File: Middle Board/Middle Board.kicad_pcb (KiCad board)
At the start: 2 copper layers, 61 parts, among them J1 JTAG Connector, J2 Conn_Coaxial, J3 Conn_Coaxial, J4 Conn_Coaxial, J5 Conn_Coaxial, J6 Conn_02x10_Counter_Clockwise, SW1 SW_SPST, U1 ATSAMG55, U2 BNO055_Breakout, U3 MS5803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

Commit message: More changes
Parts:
- moved J4 45.7 mm to (156.2, 72.0)
- moved J5 45.1 mm to (166.8, 72.0)
- moved U6 5.66 mm to (163.0, 81.0)
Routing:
- added copper zone on F.Cu, net GND
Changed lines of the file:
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@@
     (47 F.CrtYd user)
     (48 B.Fab user hide)
-    (49 F.Fab user)
+    (49 F.Fab user hide)
   )
   (setup
@@
       (effects (font (size 1 1) (thickness 0.15)))
     )
-    (fp_text value B39162B3520U410 (at 0 -3) (layer F.Fab)
+    (fp_text value B39162B3520U410 (at 0 0) (layer F.Fab)
       (effects (font (size 1 1) (thickness 0.15)))
     )
@@
   )
   (module "Custom Footprints:SMA_SMD_RIGHT_ANGLE" (layer F.Cu)
-    (at 201 63 180)
+    (at 156.23 72 180)
     (fp_text reference J4 (at 6 -2 180) (layer F.SilkS)
       (effects (font (size 1 1) (thickness 0.15)))
@@
   )
   (module "Custom Footprints:SMA_SMD_RIGHT_ANGLE" (layer F.Cu)
-    (at 211 63 180)
+    (at 166.77 72 180)
     (fp_text reference J5 (at 6 -2 180) (layer F.SilkS)
       (effects (font (size 1 1) (thickness 0.15)))
@@
   )
   (module "Custom Footprints:SMD_PD_ANAREN" (layer F.Cu)
-    (at 159 77 90)
+    (at 163 81 90)
     (fp_text reference U6 (at 4 0 90) (layer F.SilkS)
       (effects (font (size 1 1) (thickness 0.15)))
@@
       )
     )
+  )
+  (zone (net 2) (net_name GND) (layer F.Cu) (hatch edge 0.508)
+    (connect_pads (clearance 0.153))
+    (min_thickness 0.254)
+    (fill yes (arc_segments 16) (thermal_gap 0.508) (thermal_bridge_width 0.508))
+    (polygon
+      (pts
+        (xy 120 72) (xy 120 90) (xy 153 90) (xy 153 72)
+      )
+    )

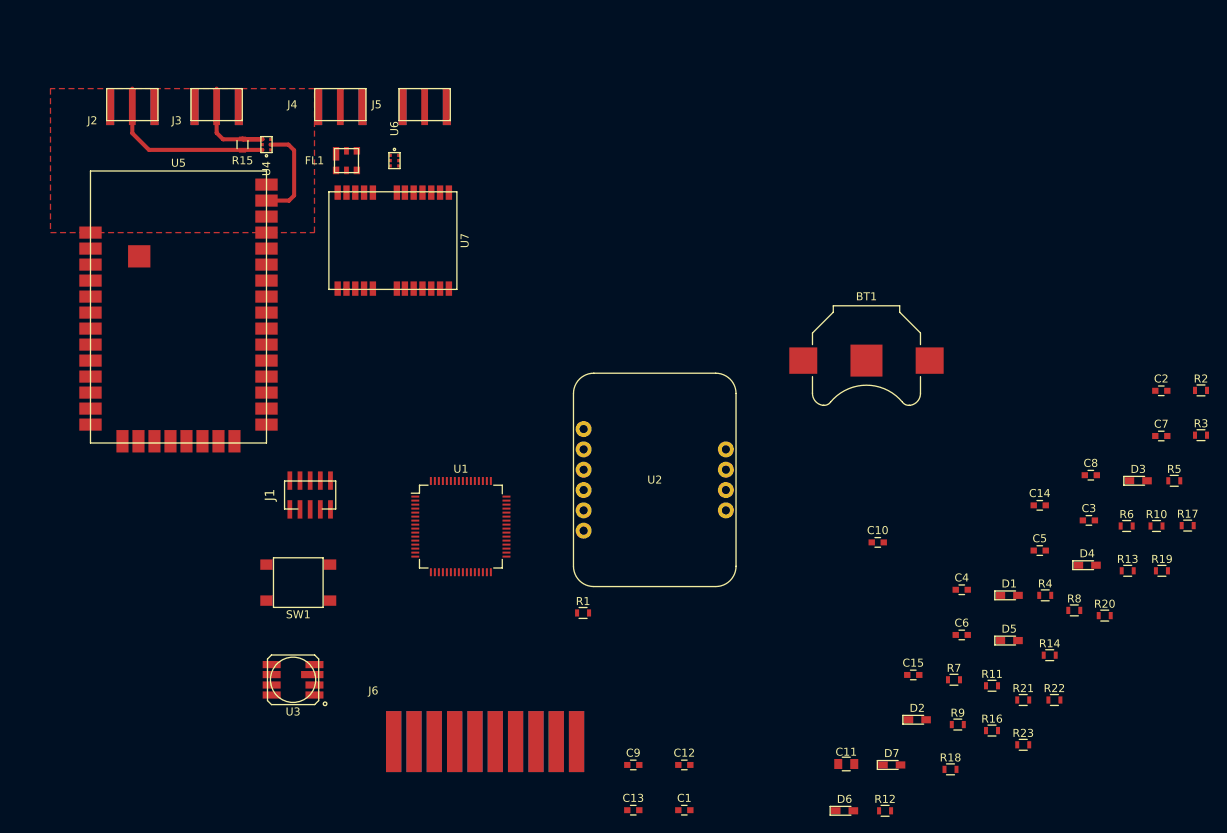
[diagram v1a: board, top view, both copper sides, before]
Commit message: Added the RS422 transceiver since I forgot it
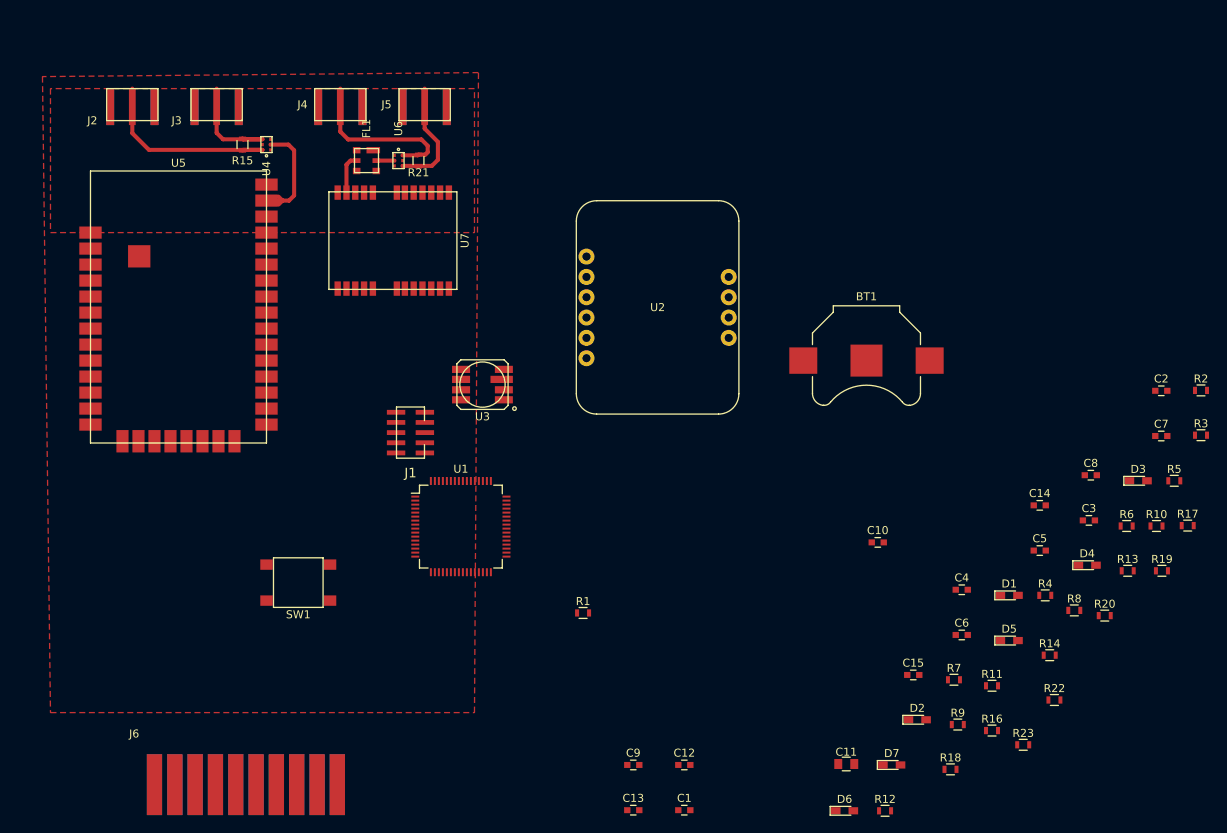
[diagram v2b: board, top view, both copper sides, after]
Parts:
- moved R21 101.3 mm to (166.0, 81.0), turned to 270 degrees
- moved U3 43.8 mm to (174.0, 109.0)
- moved J6 30.4 mm to (144.4, 162.8)
- moved U2 21.6 mm to (195.9, 99.3)
- moved J1 14.8 mm to (165.0, 115.0), turned to 90 degrees
- moved FL1 2.50 mm to (159.5, 81.0), turned to 270 degrees
- moved U6 0.50 mm to (163.5, 81.0)
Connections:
- U6 pad 1: Net-(U6-Pad1) -> GND
- U6 pad 3: Net-(U6-Pad1) -> GND
- U6 pad 5: Net-(U6-Pad1) -> GND
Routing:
- net /ANT3_RF_50Ω: track 0.00 -> 21.2 mm
- net /ANT4_RF_50Ω: track 0.00 -> 14.3 mm
- net /GPS_RF_50Ω: track 0.00 -> 4.71 mm
- net /ANT1_RF_50Ω: track 22.7 -> 25.2 mm
- net /GPS_FILT_RF_50Ω: track 0.00 -> 2.00 mm
- net /XBEE_RF_50Ω: track 12.6 -> 14.0 mm

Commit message: Removed buzzer, changed board sizes
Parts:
- moved J6 16.4 mm to (130.8, 153.7)
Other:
- board outline added: 80 x 45.7 mm
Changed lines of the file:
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@@
   (general
     (links 172)
-    (no_connects 141)
-    (area 120 67.725 265.590002 165.2)
+    (no_connects 133)
+    (area 116.764999 107.874999 196.925001 153.745001)
     (thickness 1.6)
-    (drawings 0)
+    (drawings 4)
     (tracks 37)
     (zones 0)
@@
   )
   (module "Custom Footprints:CONN_CARD_02x10_MALE" (layer F.Cu)
-    (at 144.43 162.81)
+    (at 130.81 153.67)
     (solder_mask_margin 0.381)
     (fp_text reference J6 (at -13.97 -10.16) (layer F.SilkS)
@@
       (net 2 GND))
   )
+  (gr_line (start 196.85 153.67) (end 116.84 153.67) (layer Edge.Cuts) (width 0.15))
+  (gr_line (start 196.85 107.95) (end 196.85 153.67) (layer Edge.Cuts) (width 0.15))
+  (gr_line (start 116.84 107.95) (end 196.85 107.95) (layer Edge.Cuts) (width 0.15))
+  (gr_line (start 116.84 153.67) (end 116.84 107.95) (layer Edge.Cuts) (width 0.15))
   (segment (start 161 81) (end 163 81) (width 0.5092) (layer F.Cu) (net 17))
   (segment (start 157 81.5) (end 157.5 81) (width 0.5092) (layer F.Cu) (net 18))
@@
     (min_thickness 0.254)
     (keepout (tracks not_allowed) (vias not_allowed) (copperpour not_allowed))
-    (fill (arc_segments 16) (thermal_gap 0.508) (thermal_bridge_width 0.508))
+    (fill yes (arc_segments 16) (thermal_gap 0.508) (thermal_bridge_width 0.508))
     (polygon
       (pts
@@
     (min_thickness 0.254)
     (keepout (tracks not_allowed) (vias not_allowed) (copperpour not_allowed))
-    (fill (arc_segments 16) (thermal_gap 0.508) (thermal_bridge_width 0.508))
+    (fill yes (arc_segments 16) (thermal_gap 0.508) (thermal_bridge_width 0.508))
     (polygon
       (pts

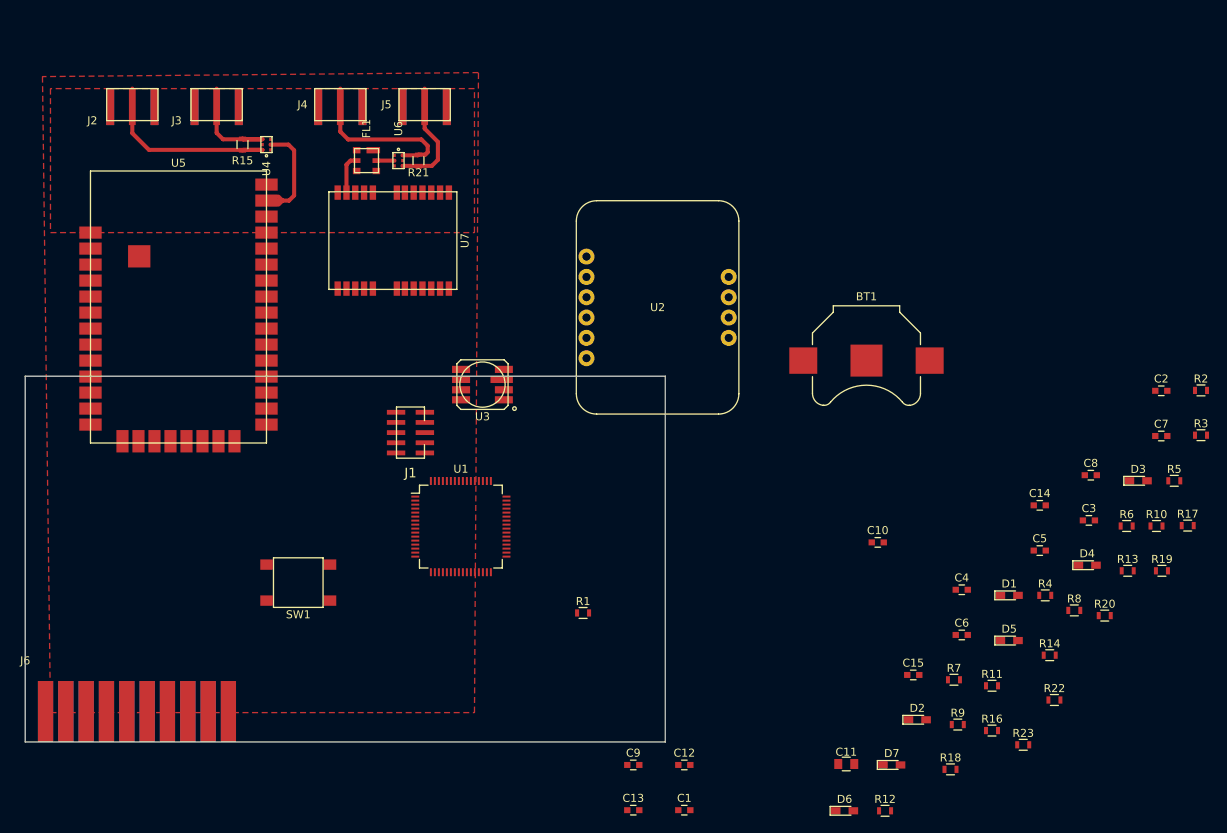
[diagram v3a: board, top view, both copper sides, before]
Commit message: Finished routing power board
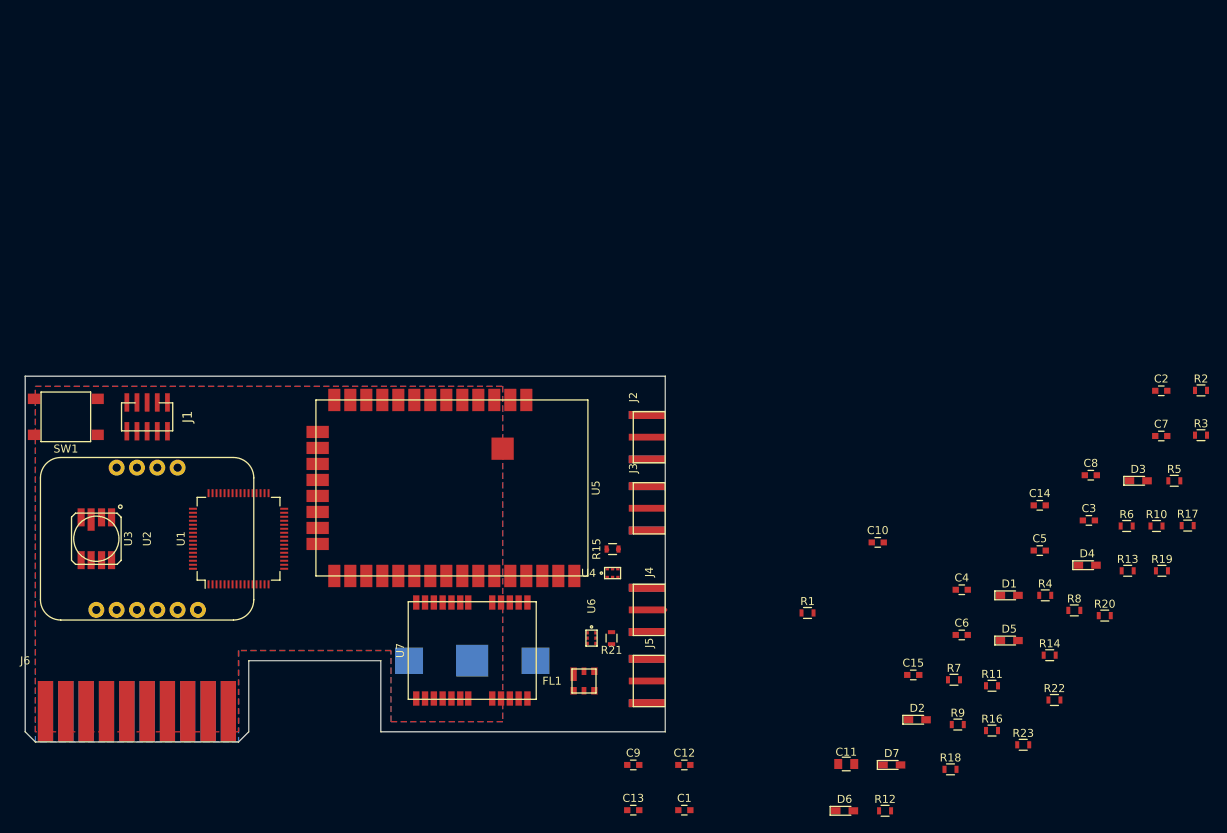
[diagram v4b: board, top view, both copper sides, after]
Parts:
- BT1: moved to B.Cu
- moved J5 79.9 mm to (196.8, 146.1), turned to 90 degrees
- moved J2 79.6 mm to (196.8, 115.6), turned to 90 degrees
- moved J3 76.8 mm to (196.8, 124.5), turned to 90 degrees
- moved J4 76.8 mm to (196.8, 137.2), turned to 90 degrees
- moved FL1 70.5 mm to (186.7, 146.1), turned to 0 degrees
- moved U2 70.1 mm to (132.1, 128.3), turned to 90 degrees
- moved U4 68.8 mm to (190.3, 132.6), turned to 180 degrees
- moved R15 68.5 mm to (190.3, 129.6), turned to 0 degrees
- moved R21 64.4 mm to (190.1, 140.7)
- moved U6 64.4 mm to (187.6, 140.7)
- moved BT1 61.9 mm to (172.7, 143.5), turned to 180 degrees
- moved U7 52.2 mm to (172.7, 142.2), turned to 270 degrees
- moved U3 52.0 mm to (125.7, 128.3), turned to 90 degrees
- moved U5 41.0 mm to (170.2, 121.9), turned to 270 degrees
- moved SW1 35.7 mm to (121.9, 113.0)
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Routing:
- net /ANT1_RF_50Ω: track 25.2 -> 0.13 mm
- net /ANT3_RF_50Ω: track 21.2 -> 3.16 mm
- net /ANT4_RF_50Ω: track 14.3 -> 0.00 mm
- net /XBEE_RF_50Ω: track 14.0 -> 0.00 mm
- net /ANT2_RF_50Ω: track 14.2 -> 0.21 mm
- net /GPS_RF_50Ω: track 4.71 -> 0.00 mm
- net /GPS_FILT_RF_50Ω: track 2.00 -> 0.00 mm
- added copper zone on B.Cu, net GND
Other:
- outline, holes or cut-outs redrawn
